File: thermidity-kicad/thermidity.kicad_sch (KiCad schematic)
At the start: 15 parts, among them J1 ISP, J2 Display, U1 ATmega328P-P, U2 MCP1501-30xSN, U3 TMP36GT9, U4 HIH-5030-001

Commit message: remove 100nF cap from humidity sensor
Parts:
- removed C6: 100nF, Capacitor_SMD:C_1206_3216Metric_Pad1.33x1.80mm_HandSolder, symbol Device:C
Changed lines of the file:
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@@
-    (pin "2")
-  )
-  (symbol (lib_id "Device:C") (at 118.11 85.09 0) (unit 1)
-    (in_bom yes) (on_board yes) (fields_autoplaced)
-    (property "Reference" "C6" (id 0) (at 121.92 83.8199 0)
-      (effects (font (size 1.27 1.27)) (justify left))
-    )
-    (property "Value" "100nF" (id 1) (at 121.92 86.3599 0)
-      (effects (font (size 1.27 1.27)) (justify left))
-    )
-    (property "Footprint" "Capacitor_SMD:C_1206_3216Metric_Pad1.33x1.80mm_HandSolder" (id 2) (at 119.0752 88.9 0)
-      (effects (font (size 1.27 1.27)) hide)
-    )
-    (property "Datasheet" "~" (id 3) (at 118.11 85.09 0)
-      (effects (font (size 1.27 1.27)) hide)
-    )
-    (pin "1")
     (pin "2")
   )
@@
       (reference "C5") (unit 1) (value "100nF") (footprint "Capacitor_SMD:C_1206_3216Metric_Pad1.33x1.80mm_HandSolder")
     )
-    (path "/db40b7f0-e6a5-4142-b519-2f92cc164ff2"
-      (reference "C6") (unit 1) (value "100nF") (footprint "Capacitor_SMD:C_1206_3216Metric_Pad1.33x1.80mm_HandSolder")
-    )
     (path "/60063fea-c781-49af-81c6-4ddf33326155"

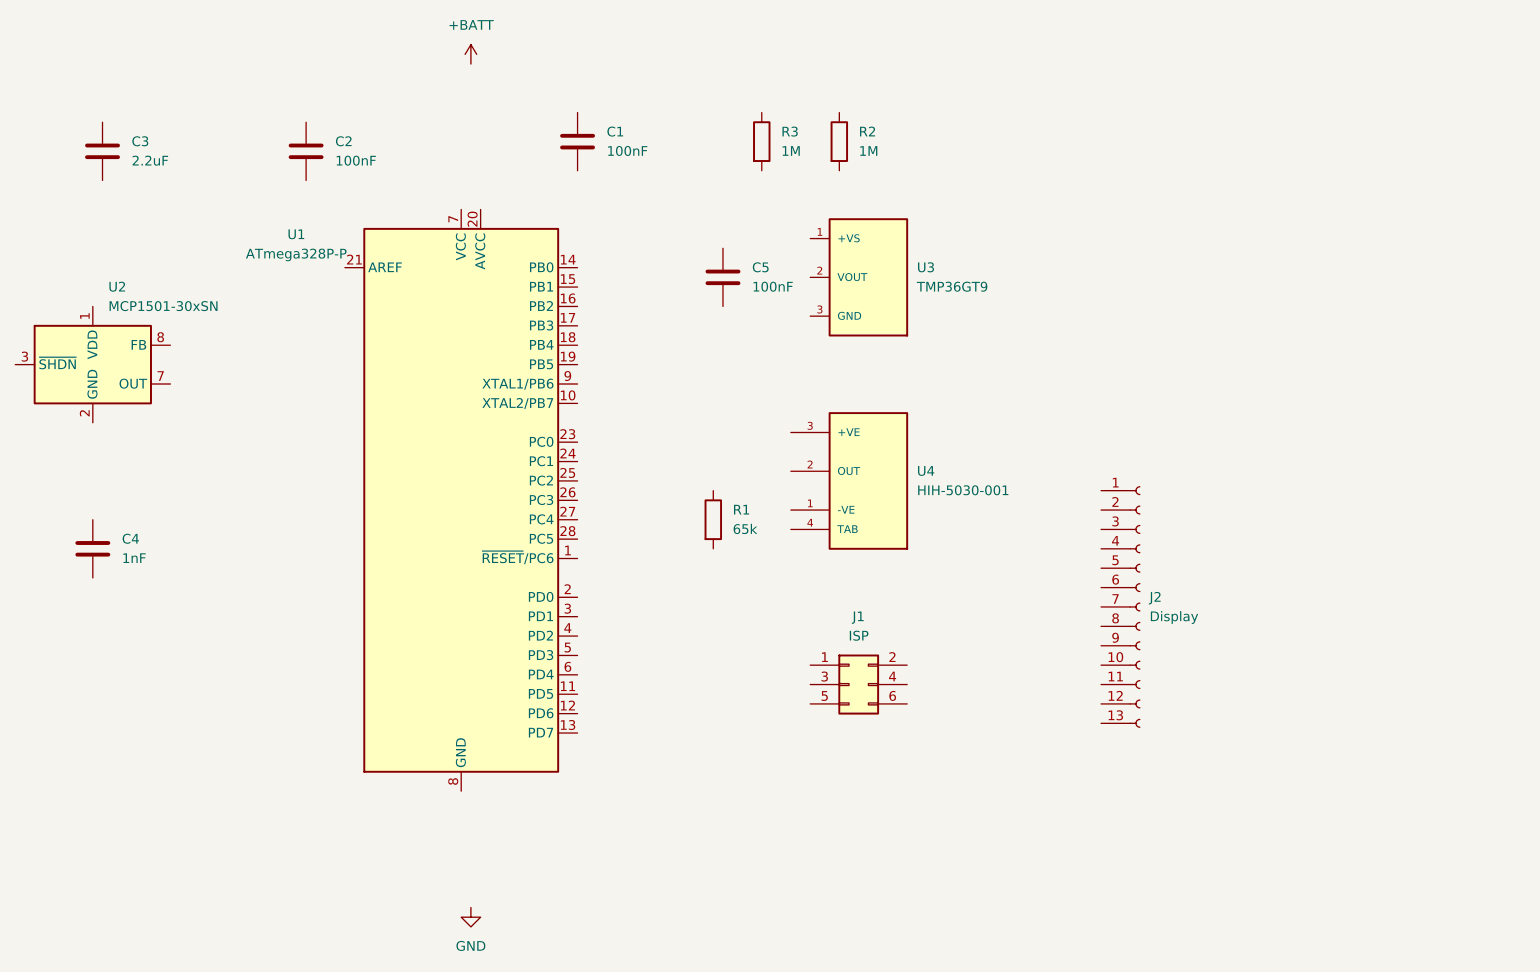
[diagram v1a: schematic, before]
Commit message: update schematic
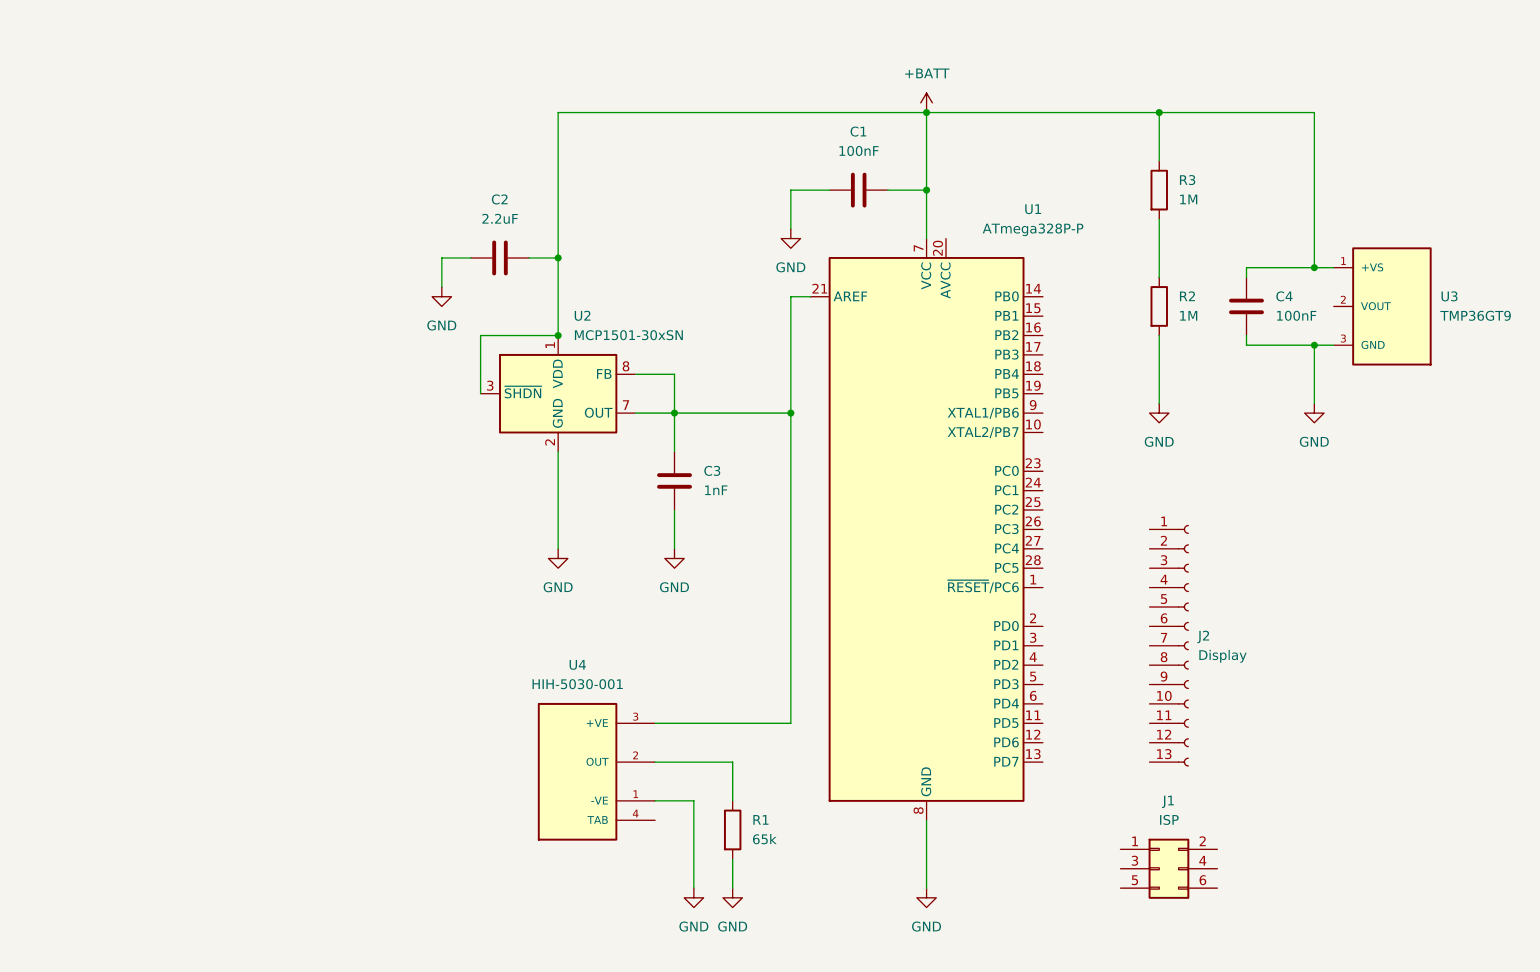
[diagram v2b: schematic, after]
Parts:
- removed C1: 100nF, Capacitor_SMD:C_1206_3216Metric_Pad1.33x1.80mm_HandSolder, symbol Device:C
- renumbered C2 to C1, C3 to C2, C4 to C3, C5 to C4
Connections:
- net +BATT: now also C1.2, C2.2, C4.1, R3.1, U1.7 (VCC), U2.1 (VDD), U2.3 (~{SHDN}), U3.1 (+VS)
- net GND: now also C1.1, C2.1, C3.2, C4.2, R1.2, R2.2, U1.22 (GND), U1.8 (GND), U2.2 (GND), U2.4 (GND), U2.5 (GND), U2.6 (GND), U3.3 (GND), U4.1 (-VE)
- net at U1.21 (AREF): now also C3.1, U2.7 (OUT), U2.8 (FB), U4.3 (+VE)
- net at R1.1: now also U4.2 (OUT)
- net at R2.1: now also R3.2
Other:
- moved on the sheet: C1, C2, C3, C4, J1, J2, R1, R2, R3, U1, U2, U3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
